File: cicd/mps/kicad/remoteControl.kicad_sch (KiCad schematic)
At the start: 26 parts, among them J1 Conn_01x02, J2 USB_2, P1 CONN_1, P10 CONN_2, P11 CONN_1, P12 CONN_1, P13 CONN_1, P14 CONN_3, P15 CONN_1, P16 CONN_1, P17 CONN_1, P18 CONN_1, P19 CONN_1, P2 CONN_1, P3 PI, P4 CONN_5, P5 CONN_1, P6 CONN_3, P7 CONN_4X1, P8 CONN_2, P9 CONN_2, U1 BUCK

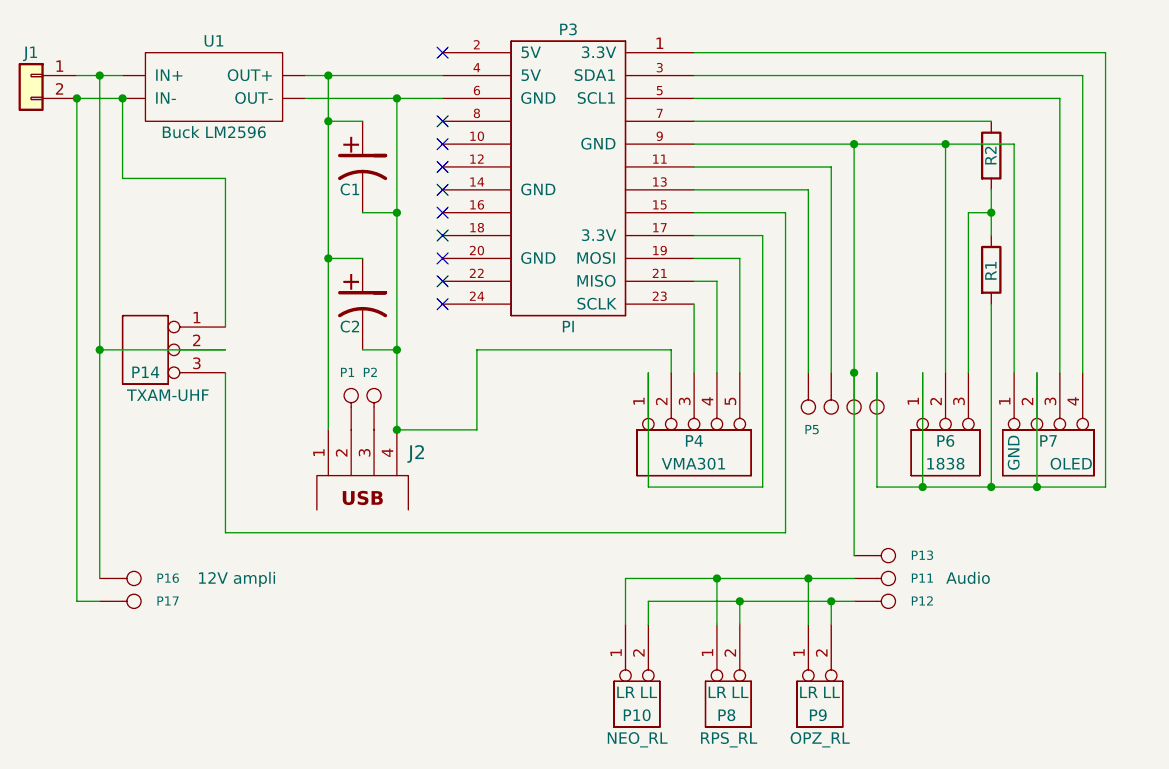
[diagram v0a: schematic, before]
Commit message: mps/kicad: frees up the SPI pins
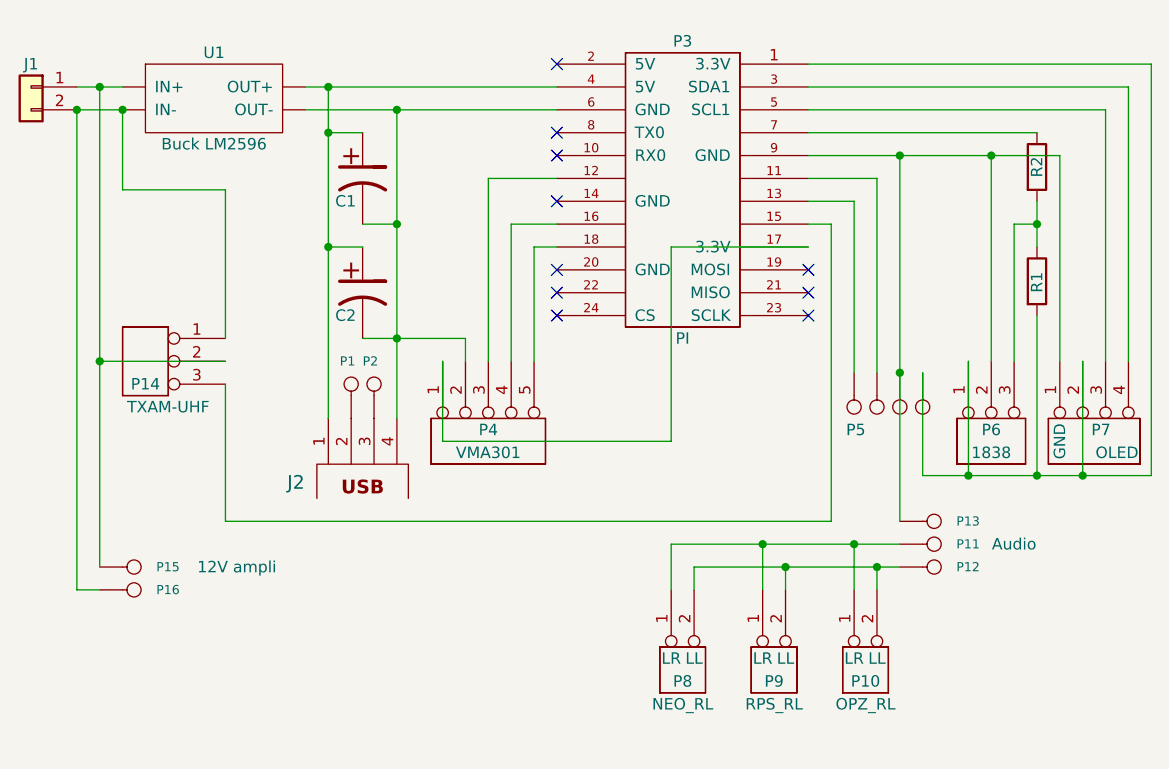
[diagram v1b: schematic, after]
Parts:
- renumbered P9 to P10, P16 to P15, P17 to P16, P15 to P17, P10 to P8, P8 to P9
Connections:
- net at P4.3 (P3): now also P3.12; no longer P3.23 (SCLK)
- net at P4.4 (P4): now also P3.16; no longer P3.21 (MISO)
- net at P4.5 (P5): now also P3.18; no longer P3.19 (MOSI)
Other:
- moved on the sheet: C1, C2, J1, J2, P1, P10, P11, P12, P13, P14, P15, P16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

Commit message: mps: update kicad files for pigpio-spi
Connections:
- net at P3.15: no longer P14.3 (P3)
- net at P3.19 (MOSI): now also P14.3 (P3)
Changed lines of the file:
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@@
 	)
 	(no_connect
-		(at 172.72 92.71)
+		(at 172.72 87.63)
 	)
 	(no_connect
@@
 	(wire
 		(pts
+			(xy 175.26 92.71) (xy 175.26 120.65)
+		)
+		(stroke
+			(width 0)
+			(type default)
+		)
+	)
+	(wire
+		(pts
 			(xy 132.08 111.76) (xy 157.48 111.76)
 		)
@@
 	(wire
 		(pts
-			(xy 172.72 87.63) (xy 175.26 87.63)
+			(xy 172.72 92.71) (xy 175.26 92.71)
 		)
 		(stroke
@@
 		)
 		(stroke
-			(width 0)
-			(type default)
-		)
-	)
-	(wire
-		(pts
-			(xy 175.26 87.63) (xy 175.26 120.65)
-		)
-		(stroke
